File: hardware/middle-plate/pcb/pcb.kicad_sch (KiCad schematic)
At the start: 118 parts, among them SW1 MT-0-102-A101-M200-RS+PJ, SW2 TS4535TP 250GF 009, SW3 TS4535TP 250GF 009, SW4 TS4535TP 250GF 009, SW5 TS4535TP 250GF 009, SW6 TS4535TP 250GF 009, SW7 TS4535TP 250GF 009

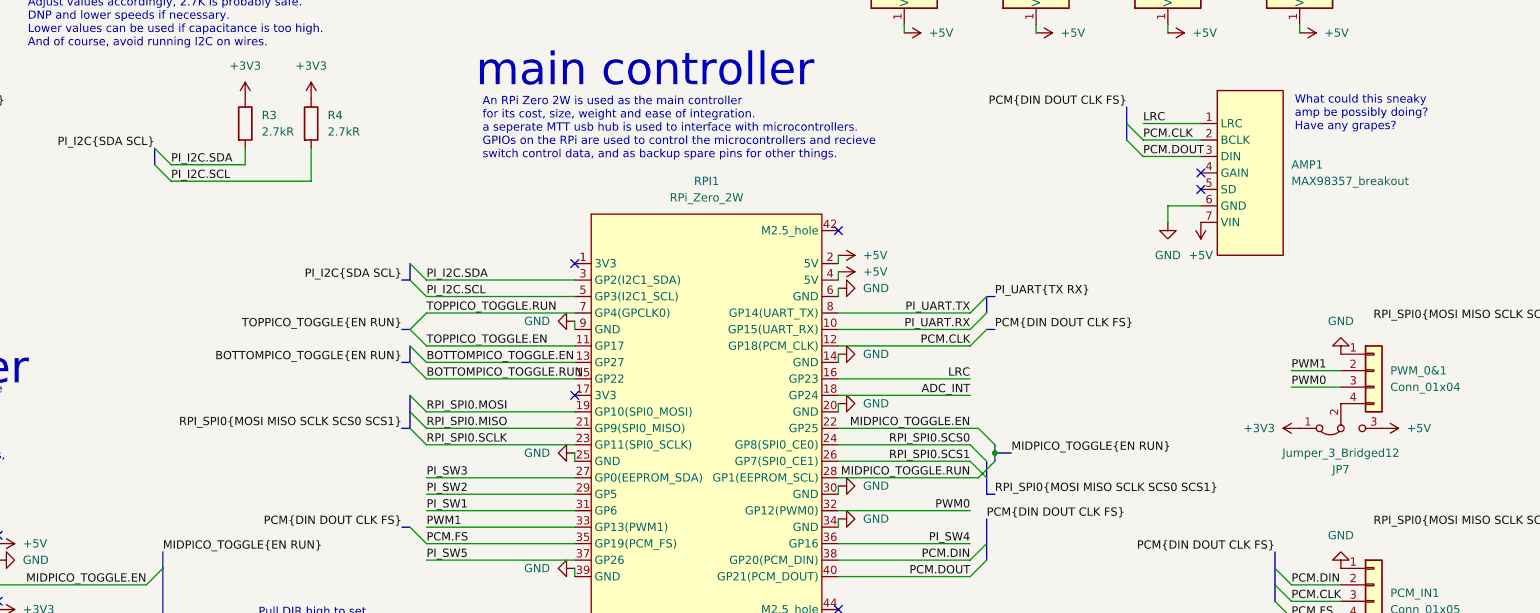
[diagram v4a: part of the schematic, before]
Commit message: fixed up symbols and footprints for top plate, and completed top plate schematic (other than modifications for better routing)
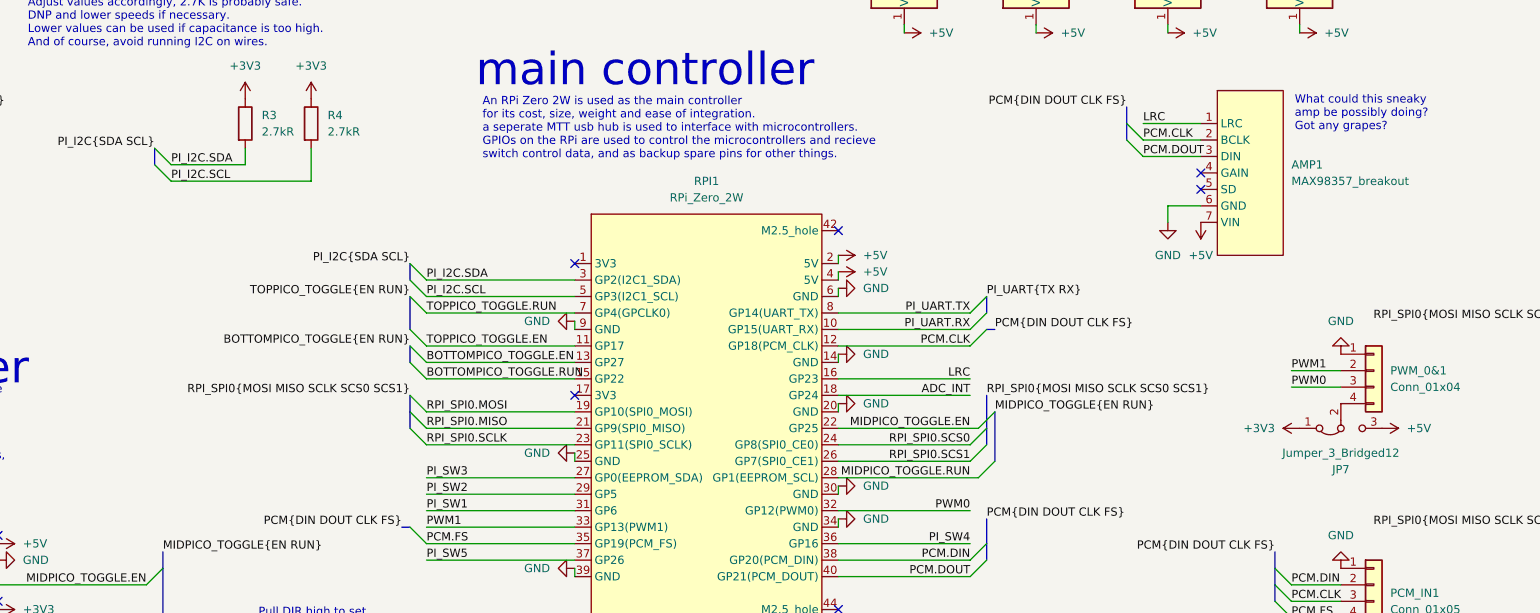
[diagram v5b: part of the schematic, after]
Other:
- note added: "What could this sneaky amp be possibly doing? Got any grapes?"
- note removed: "What could this sneaky amp be possibly doing? Have any grapes?"
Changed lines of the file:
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@@
 	)
 	(junction
-		(at 229.87 210.82)
-		(diameter 0)
-		(color 0 0 0 0)
-	)
-	(junction
 		(at 337.82 30.48)
 		(diameter 0)
@@
 	)
 	(bus_entry
-		(at 318.77 139.7)
-		(size 2.54 2.54)
+		(at 228.6 209.55)
+		(size -2.54 2.54)
 		(stroke
 			(width 0)
@@
 	)
 	(bus_entry
-		(at 312.42 127)
+		(at 318.77 139.7)
 		(size 2.54 2.54)
 		(stroke
@@
 	)
 	(bus_entry
-		(at 228.6 214.63)
-		(size -2.54 -2.54)
+		(at 312.42 127)
+		(size 2.54 2.54)
 		(stroke
 			(width 0)
@@
 	)
 	(bus_entry
+		(at 142.24 189.23)
+		(size -2.54 -2.54)
+		(stroke
+			(width 0)
+			(type default)
+		)
+	)
+	(bus_entry
 		(at 322.58 193.04)
 		(size 2.54 2.54)
@@
 	)
 	(bus_entry
-		(at 229.87 209.55)
-		(size -2.54 -2.54)
-		(stroke
-			(width 0)
-			(type default)
-		)
-	)
-	(bus_entry
-		(at 139.7 191.77)
-		(size 2.54 -2.54)
+		(at 229.87 204.47)
+		(size -2.54 2.54)
 		(stroke
 			(width 0)
@@
 	)
 	(bus_entry
-		(at 228.6 212.09)
-		(size -2.54 -2.54)
-		(stroke
-			(width 0)
-			(type default)
-		)
-	)
-	(bus_entry
 		(at 273.05 233.68)
 		(size 2.54 2.54)
@@
 	)
 	(bus_entry
+		(at 228.6 207.01)
+		(size -2.54 2.54)
+		(stroke
+			(width 0)
+			(type default)
+		)
+	)
+	(bus_entry
 		(at 322.58 224.79)
 		(size 2.54 2.54)
@@
 		)
 	)
-	(bus
-		(pts
-			(xy 139.7 201.93) (xy 139.7 204.47)
-		)
-		(stroke
-			(width 0)
-			(type default)
-		)
-	)
 	(wire
 		(pts
@@
 		)
 	)
-	(bus
-		(pts
-			(xy 232.41 210.82) (xy 229.87 210.82)
-		)
-		(stroke
-			(width 0)
-			(type default)
-		)
-	)
 	(wire
 		(pts
@@
 		)
 	)
-	(bus
-		(pts
-			(xy 139.7 191.77) (xy 138.43 191.77)
-		)
-		(stroke
-			(width 0)
-			(type default)
-		)
-	)
 	(wire
 		(pts
@@
 		)
 	)
-	(bus
-		(pts
-			(xy 228.6 214.63) (xy 228.6 212.09)
-		)
-		(stroke
-			(width 0)
-			(type default)
-		)
-	)
 	(wire
 		(pts
@@
 		)
 	)
+	(bus
+		(pts
+			(xy 139.7 194.31) (xy 139.7 196.85)
+		)
+		(stroke
+			(width 0)
+			(type default)
+		)
+	)
 	(wire
 		(pts
@@
 	(bus
 		(pts
-			(xy 228.6 217.17) (xy 228.6 214.63)
+			(xy 228.6 201.93) (xy 228.6 207.01)
 		)
 		(stroke
@@
 		)
 	)
-	(bus
-		(pts
-			(xy 229.87 217.17) (xy 228.6 217.17)
-		)
-		(stroke
-			(width 0)
-			(type default)
-		)
-	)
 	(wire
 		(pts
@@
 		)
 	)
-	(wire
+	(bus
 		(pts
-			(xy 269.24 55.88) (xy 264.16 55.88)
+			(xy 229.87 204.47) (xy 229.87 212.09)
 		)
 		(stroke
@@
 		)
 	)
-	(bus
+	(wire
 		(pts
-			(xy 320.04 147.32) (xy 318.77 147.32)
+			(xy 269.24 55.88) (xy 264.16 55.88)
 		)
 		(stroke
@@
 		)
 	)
-	(wire
+	(bus
 		(pts
-			(xy 256.54 44.45) (xy 256.54 43.18)
+			(xy 320.04 147.32) (xy 318.77 147.32)
 		)
 		(stroke
@@
 		)
 	)
-	(bus
+	(wire
 		(pts
-			(xy 138.43 207.01) (xy 139.7 207.01)
+			(xy 256.54 44.45) (xy 256.54 43.18)
 		)
 		(stroke
@@
 		)
 	)
-	(bus
+	(wire
 		(pts
-			(xy 229.87 191.77) (xy 228.6 191.77)
+			(xy 276.86 67.31) (xy 276.86 68.58)
 		)
 		(stroke
@@
 	(wire
 		(pts
-			(xy 276.86 67.31) (xy 276.86 68.58)
+			(xy 48.26 162.56) (xy 48.26 168.91)
 		)
 		(stroke
@@
 		)
 	)
-	(wire
+	(bus
 		(pts
-			(xy 48.26 162.56) (xy 48.26 168.91)
+			(xy 229.87 191.77) (xy 228.6 191.77)
 		)
 		(stroke
@@
 		)
 	)
-	(bus
-		(pts
-			(xy 138.43 196.85) (xy 139.7 196.85)
-		)
-		(stroke
-			(width 0)
-			(type default)
-		)
-	)
 	(wire
 		(pts
@@
 		)
 	)
+	(bus
+		(pts
+			(xy 139.7 204.47) (xy 139.7 207.01)
+		)
+		(stroke
+			(width 0)
+			(type default)
+		)
+	)
 	(wire
 		(pts
@@
 		)
 	)
-	(bus
-		(pts
-			(xy 138.43 184.15) (xy 139.7 184.15)
-		)
-		(stroke
-			(width 0)
-			(type default)
-		)
-	)
 	(wire
 		(pts
@@
 		)
 	)
-	(bus
-		(pts
-			(xy 229.87 210.82) (xy 229.87 212.09)
-		)
-		(stroke
-			(width 0)
-			(type default)
-		)
-	)
 	(wire
 		(pts
@@
 		)
 	)
-	(bus
-		(pts
-			(xy 229.87 186.69) (xy 228.6 186.69)
-		)
-		(stroke
-			(width 0)
-			(type default)
-		)
-	)
 	(wire
 		(pts
@@
 	(bus
 		(pts
-			(xy 139.7 207.01) (xy 139.7 204.47)
+			(xy 139.7 201.93) (xy 139.7 204.47)
 		)
 		(stroke
@@
 		)
 	)
+	(bus
+		(pts
+			(xy 139.7 186.69) (xy 139.7 191.77)
+		)
+		(stroke
+			(width 0)
+			(type default)
+		)
+	)
 	(wire
 		(pts
@@
 		)
 	)
-	(bus
+	(wire
 		(pts
-			(xy 229.87 209.55) (xy 229.87 210.82)
+			(xy 337.82 76.2) (xy 358.14 76.2)
 		)
 		(stroke
@@
 	(wire
 		(pts
-			(xy 337.82 76.2) (xy 358.14 76.2)
+			(xy 378.46 83.82) (xy 398.78 83.82)
 		)
 		(stroke
@@
 	(wire
 		(pts
-			(xy 378.46 83.82) (xy 398.78 83.82)
+			(xy 321.31 154.94) (xy 342.9 154.94)
 		)
 		(stroke
@@
 	(wire
 		(pts
-			(xy 321.31 154.94) (xy 342.9 154.94)
+			(xy 269.24 96.52) (xy 264.16 96.52)
 		)
 		(stroke
@@
 		)
 	)
-	(wire
+	(bus
 		(pts
-			(xy 269.24 96.52) (xy 264.16 96.52)
+			(xy 228.6 207.01) (xy 228.6 209.55)
 		)
 		(stroke
@@
 		)
 	)
-	(bus
-		(pts
-			(xy 139.7 194.31) (xy 139.7 196.85)
-		)
-		(stroke
-			(width 0)
-			(type default)
-		)
-	)
 	(wire
 		(pts
@@
 		)
 	)
-	(text "What could this sneaky\namp be possibly doing?\nHave any grapes?"
+	(text "What could this sneaky\namp be possibly doing?\nGot any grapes?"
 		(exclude_from_sim no)
 		(at 276.098 158.496 0)
@@
 	)
 	(label "RPI_SPI0{MOSI MISO SCLK SCS0 SCS1}"
-		(at 138.43 207.01 180)
+		(at 139.7 201.93 180)
 		(fields_autoplaced yes)
 		(effects
@@
 	)
 	(label "PI_I2C{SDA SCL}"
-		(at 138.43 184.15 180)
+		(at 139.7 181.61 180)
 		(fields_autoplaced yes)
 		(effects
@@
 	)
 	(label "MIDPICO_TOGGLE{EN RUN}"
-		(at 232.41 210.82 0)
+		(at 229.87 204.47 0)
 		(fields_autoplaced yes)
 		(effects
@@
 	)
 	(label "TOPPICO_TOGGLE{EN RUN}"
-		(at 138.43 191.77 180)
+		(at 139.7 186.69 180)
 		(fields_autoplaced yes)
 		(effects
@@
 	)
 	(label "BOTTOMPICO_TOGGLE{EN RUN}"
-		(at 138.43 196.85 180)
+		(at 139.7 194.31 180)
 		(fields_autoplaced yes)
 		(effects
@@
 	)
 	(label "PI_UART{TX RX}"
-		(at 229.87 186.69 0)
+		(at 228.6 186.69 0)
 		(fields_autoplaced yes)
 		(effects
@@
 	)
 	(label "RPI_SPI0{MOSI MISO SCLK SCS0 SCS1}"
-		(at 229.87 217.17 0)
+		(at 228.6 201.93 0)
 		(fields_autoplaced yes)
 		(effects

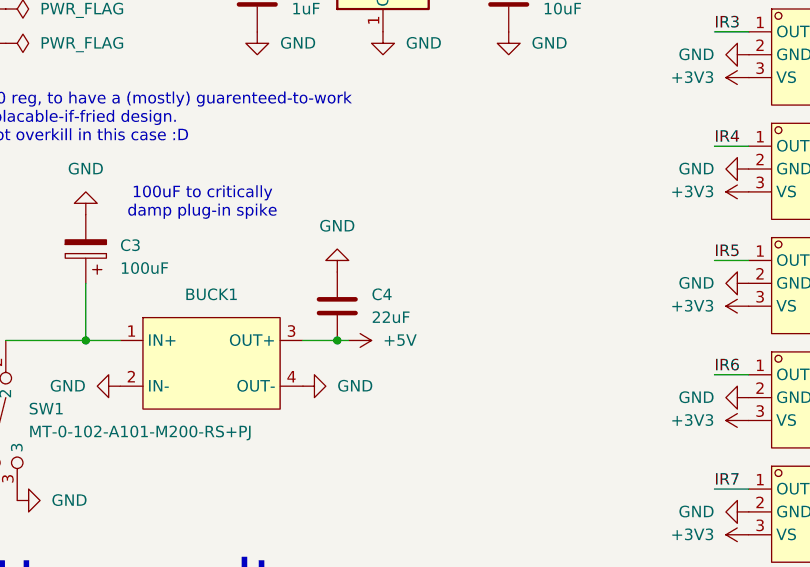
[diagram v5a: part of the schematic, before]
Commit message: added fuse to middle plate and fixed switches 3d view
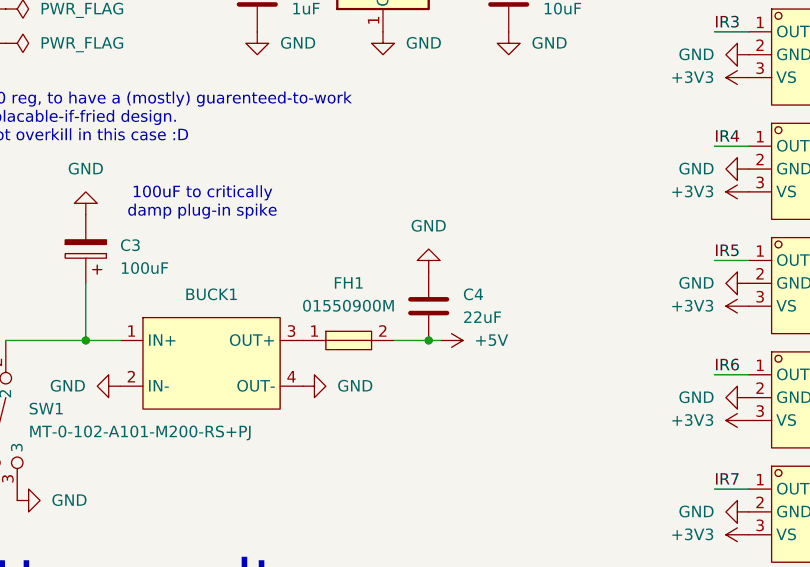
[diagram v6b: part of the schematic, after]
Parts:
- added FH1: 01550900M, EasyEDA:FUSE-SMD_L9.8-W5.0, symbol EasyEDA:01550900M
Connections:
- net +5V: now also FH1.2; no longer BUCK1.3 (OUT+)
- new net: BUCK1.3 (OUT+), FH1.1
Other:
- moved on the sheet: C4
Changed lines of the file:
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@@
 	)
 	(junction
-		(at 62.23 88.9)
-		(diameter 0)
-		(color 0 0 0 0)
-	)
-	(junction
 		(at 337.82 30.48)
 		(diameter 0)
@@
 	)
 	(junction
+		(at 72.39 88.9)
+		(diameter 0)
+		(color 0 0 0 0)
+	)
+	(junction
 		(at 378.46 93.98)
 		(diameter 0)
@@
 	(wire
 		(pts
-			(xy 62.23 88.9) (xy 58.42 88.9)
-		)
-		(stroke
-			(width 0)
-			(type default)
-		)
-	)
-	(wire
-		(pts
 			(xy 252.73 165.1) (xy 261.62 165.1)
 		)
@@
 	(wire
 		(pts
-			(xy 63.5 88.9) (xy 62.23 88.9)
+			(xy 73.66 88.9) (xy 72.39 88.9)
 		)
 		(stroke
@@
 	(wire
 		(pts
+			(xy 68.58 88.9) (xy 72.39 88.9)
+		)
+		(stroke
+			(width 0)
+			(type default)
+		)
+	)
+	(wire
+		(pts
 			(xy 215.9 146.05) (xy 215.9 144.78)
 		)
@@
 	(symbol
 		(lib_id "power:GND")
-		(at 62.23 81.28 180)
+		(at 72.39 81.28 180)
 		(unit 1)
 		(exclude_from_sim no)
@@
 		(fields_autoplaced yes)
 		(property "Reference" "#PWR031"
-			(at 62.23 74.93 0)
+			(at 72.39 74.93 0)
 			(effects
 				(font
@@
 		)
 		(property "Value" "GND"
-			(at 62.23 76.2 0)
+			(at 72.39 76.2 0)
 			(effects
 				(font
@@
 		)
 		(property "Footprint" ""
-			(at 62.23 81.28 0)
+			(at 72.39 81.28 0)
 			(effects
 				(font
@@
 		)
 		(property "Datasheet" ""
-			(at 62.23 81.28 0)
+			(at 72.39 81.28 0)
 			(effects
 				(font
@@
 		)
 		(property "Description" "Power symbol creates a global label with name \"GND\" , ground"
-			(at 62.23 81.28 0)
+			(at 72.39 81.28 0)
 			(effects
 				(font
@@
 	(symbol
 		(lib_id "Device:C")
-		(at 62.23 85.09 0)
+		(at 72.39 85.09 0)
 		(mirror y)
 		(unit 1)
@@
 		(fields_autoplaced yes)
 		(property "Reference" "C4"
-			(at 66.04 83.8199 0)
+			(at 76.2 83.8199 0)
 			(effects
 				(font
@@
 		)
 		(property "Value" "22uF"
-			(at 66.04 86.3599 0)
+			(at 76.2 86.3599 0)
 			(effects
 				(font
@@
 		)
 		(property "Footprint" "PCM_Capacitor_SMD_AKL:C_0805_2012Metric_Pad1.15x1.40mm_HandSolder"
-			(at 61.2648 88.9 0)
+			(at 71.4248 88.9 0)
 			(effects
 				(font
@@
 		)
 		(property "Datasheet" "~"
-			(at 62.23 85.09 0)
+			(at 72.39 85.09 0)
 			(effects
 				(font
@@
 		)
 		(property "Description" "Unpolarized capacitor"
-			(at 62.23 85.09 0)
+			(at 72.39 85.09 0)
 			(effects
 				(font
@@
 	(symbol
 		(lib_id "power:+5V")
-		(at 63.5 88.9 270)
+		(at 73.66 88.9 270)
 		(mirror x)
 		(unit 1)
@@
 		(fields_autoplaced yes)
 		(property "Reference" "#PWR032"
-			(at 59.69 88.9 0)
+			(at 69.85 88.9 0)
 			(effects
 				(font
@@
 		)
 		(property "Value" "+5V"
-			(at 67.31 88.8999 90)
+			(at 77.47 88.8999 90)
 			(effects
 				(font
@@
 		)
 		(property "Footprint" ""
-			(at 63.5 88.9 0)
+			(at 73.66 88.9 0)
 			(effects
 				(font
@@
 		)
 		(property "Datasheet" ""
-			(at 63.5 88.9 0)
+			(at 73.66 88.9 0)
 			(effects
 				(font
@@
 		)
 		(property "Description" "Power symbol creates a global label with name \"+5V\""
-			(at 63.5 88.9 0)
+			(at 73.66 88.9 0)
 			(effects
 				(font
@@
 					(unit 1)
 				)
+			)
+		)
+	)
+	(symbol
+		(lib_id "EasyEDA:01550900M")
+		(at 63.5 88.9 0)
+		(unit 1)
+		(exclude_from_sim no)
+		(in_bom yes)
+		(on_board yes)
+		(dnp no)
+		(fields_autoplaced yes)
+		(property "Reference" "FH1"
+			(at 63.5 82.55 0)
+			(effects
+				(font
+					(size 1.27 1.27)
+				)
+			)
+		)
+		(property "Value" "01550900M"
+			(at 63.5 85.09 0)
+			(effects
+				(font
+					(size 1.27 1.27)
+				)
+			)
+		)
+		(property "Footprint" "EasyEDA:FUSE-SMD_L9.8-W5.0"
+			(at 63.5 96.52 0)
+			(effects
+				(font
+					(size 1.27 1.27)
+				)
+				(hide yes)
+			)
+		)
+		(property "Datasheet" "https://lcsc.com/product-detail/Others_Littelfuse_01550900M_Littelfuse-01550900M_C108518.html"
+			(at 63.5 99.06 0)
+			(effects
+				(font
+					(size 1.27 1.27)
+				)
+				(hide yes)
+			)
+		)
+		(property "Description" ""
+			(at 63.5 88.9 0)
+			(effects
+				(font
+					(size 1.27 1.27)
+				)
+				(hide yes)
+			)
+		)
+		(property "LCSC Part" "C108518"
+			(at 63.5 101.6 0)
+			(effects
+				(font
+					(size 1.27 1.27)
+				)
+				(hide yes)
+			)
+		)
+		(pin "2"
+		)
+		(pin "1"
+		)
+		(instances
+			(project "pcb"
+				(path "/9bb3e9c6-12db-4b47-aa39-b193ca752b9a"
+					(reference "FH1")
+					(unit 1)
+				)

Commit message: labelled bottom middle and top pcbs, added testpoints
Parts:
- added 3V3TP1, 5VTP1, GNDTP1, VCCTP1: TestPoint, TestPoint:TestPoint_THTPad_D1.0mm_Drill0.5mm, symbol Connector:TestPoint
- PWR2: value XT30-F -> Conn_01x02; footprint Connector_AMASS:AMASS_XT30U-F_1x02_P5.0mm_Vertical -> Connector_JST:JST_XH_B2B-XH-A_1x02_P2.50mm_Vertical
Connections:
- net +3V3: now also 3V3TP1.1
- net +5V: now also 5VTP1.1
- net GND: now also GNDTP1.1
- net VCC: now also VCCTP1.1
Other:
- note added: "Power to top plate. JST-XH to match JST-XH of top plate. No XT30 on top plate due to height constraints and if sideways, space constraints."
- note added: "spare pins"
- note added: "testpoints"
- note removed: "Power to top plate. XT30 is overkill, but indicative and convenient. Also allows everything to be easily tested seperately. Also not much bigger than JST-XH (3A)."
